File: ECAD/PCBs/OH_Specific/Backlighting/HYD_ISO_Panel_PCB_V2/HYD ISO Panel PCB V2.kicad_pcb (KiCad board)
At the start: 2 copper layers, 104.3 x 38.9 mm, 50 parts, among them J1 Conn_01x04_Female, J2 Conn_01x04_Female

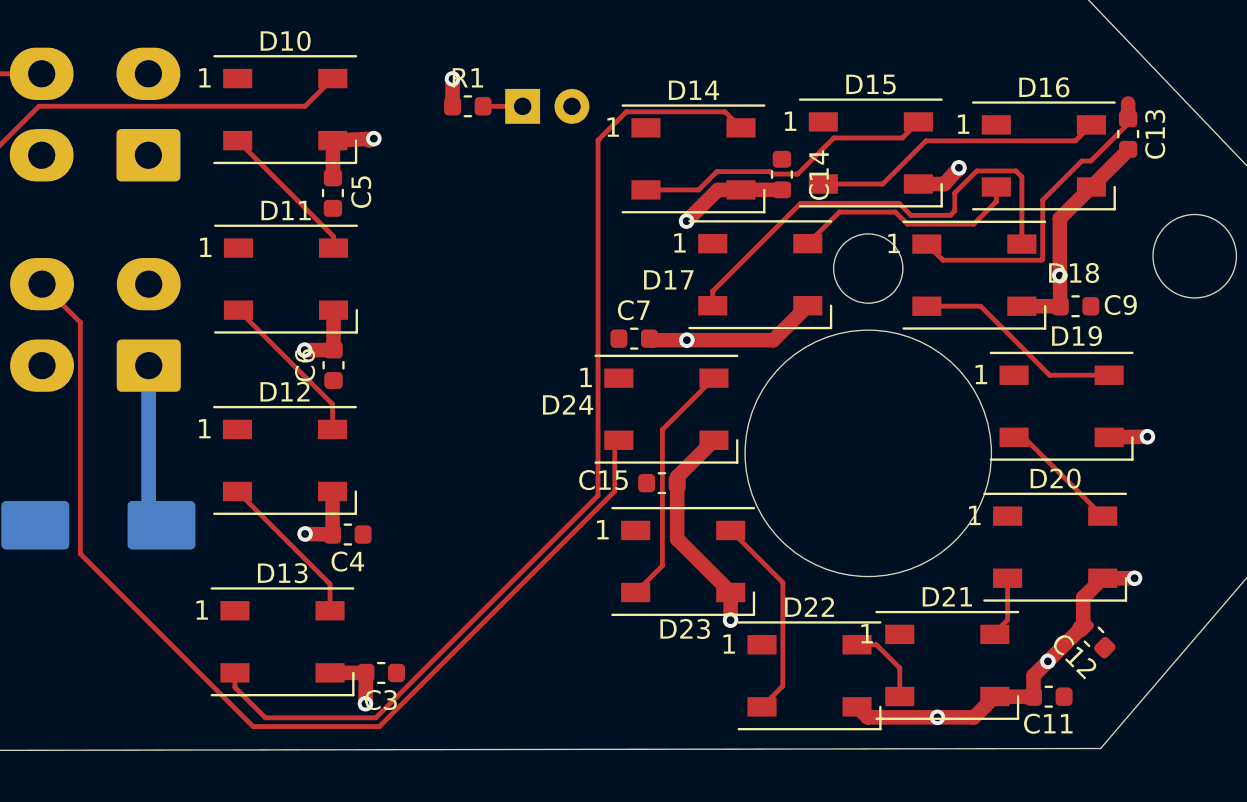
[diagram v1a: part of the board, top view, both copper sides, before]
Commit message: HYD ISO Backlighting PCB Update
Changed - Swapped MC and HYD ISO silkscreen labels
Changed - Swapped 3 and 2 position switch silkscreen labels
Changed - version to 2.1
Changed - Solid copper fills to thermal relief for LEDs, connectors remain with solid pads.
Removed - Excess crap out of folder and tidied manufacturing folder.
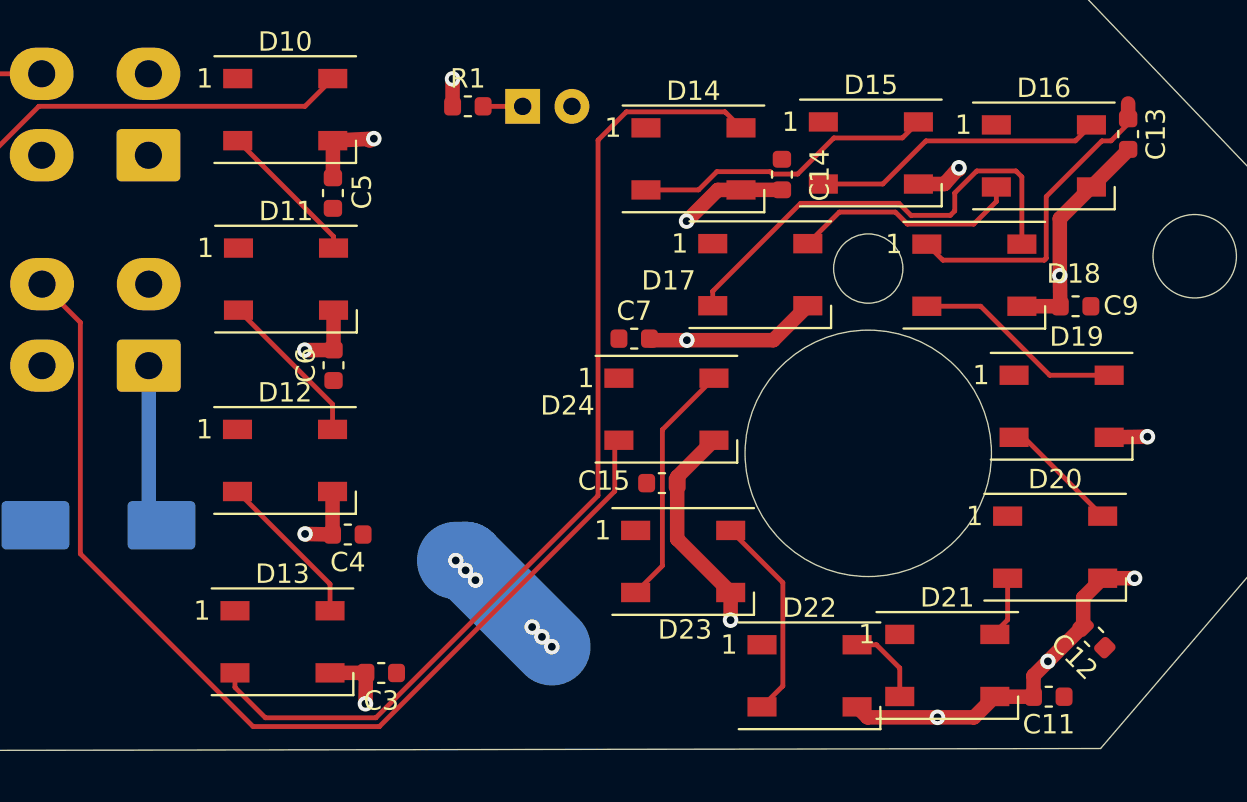
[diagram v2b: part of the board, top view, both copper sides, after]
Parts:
- moved G*** 5.48 mm to (137.3, 84.3)
- moved G*** 3.36 mm to (78.9, 83.9)
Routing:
- net /LED+5V: track 25.0 -> 31.8 mm, vias 0 -> 6
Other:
- rule pad_to_mask_clearance: 0.05 -> 0
- board text added: "Version 2.1"
- board text removed: "Version 2.0"

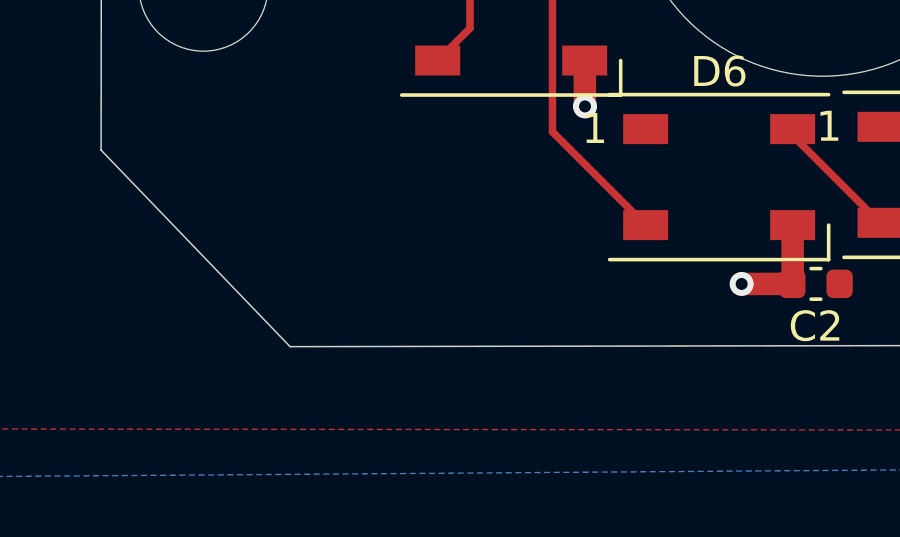
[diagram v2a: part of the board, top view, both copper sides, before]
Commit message: HYD ISO Panel Backlighting Silkscreen Improvements
Added - JLC order number location silkscreen.
Changed - Rotation of 1000uF silkscreen so it doesn't get cut off by the pad solder.
Changed - Version to 2.2
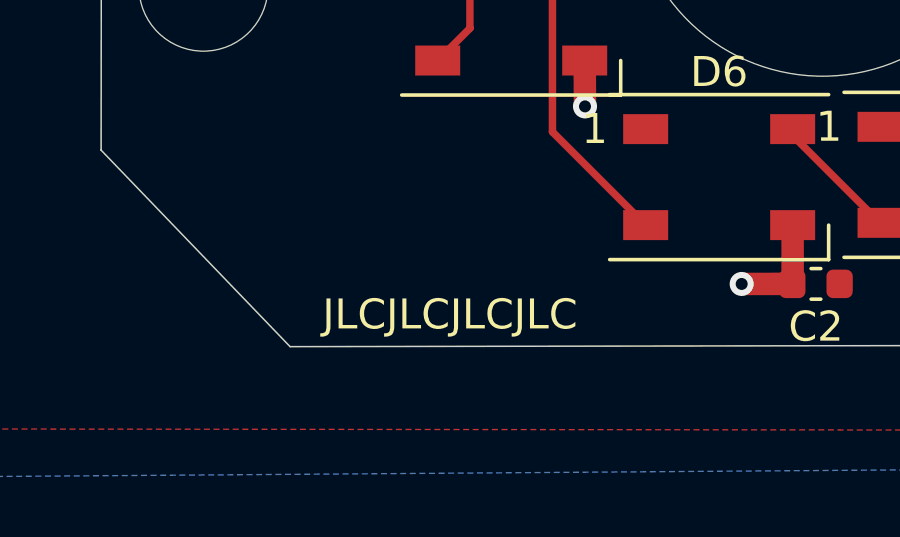
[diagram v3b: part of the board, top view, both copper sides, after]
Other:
- board text added: "JLCJLCJLCJLC"
- board text added: "Version 2.2"
- board text removed: "Version 2.1"
